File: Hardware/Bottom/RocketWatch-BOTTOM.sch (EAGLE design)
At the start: 31 parts, among them U1 AD5242-SO16

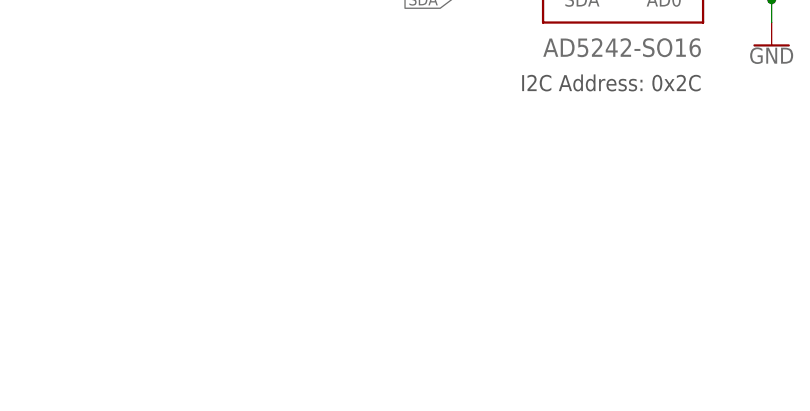
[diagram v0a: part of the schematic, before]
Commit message: changed schematic and board based on video take 002
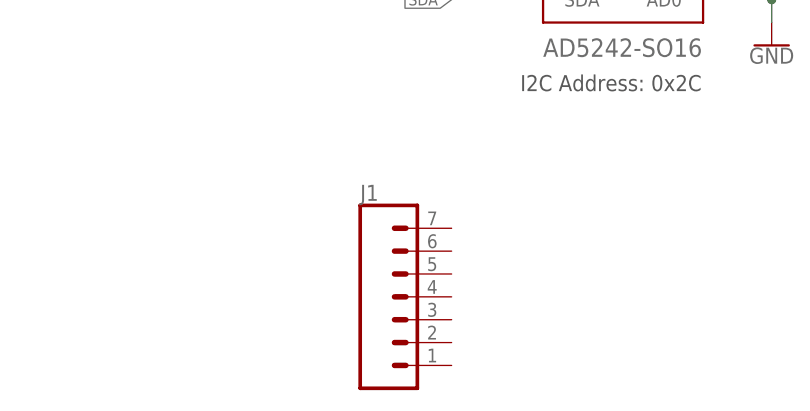
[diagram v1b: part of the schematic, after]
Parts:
- added J1: (no value), LinnesLab-Connectors:CONN_07
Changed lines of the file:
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@@
 <part name="GND30" library="LinnesLab-Symbols" deviceset="GND" device=""/>
 <part name="SUPPLY24" library="LinnesLab-Symbols" deviceset="3.3V" device=""/>
+<part name="J1" library="LinnesLab-Connectors" deviceset="CONN_07" device=""/>
 </parts>
 <sheets>
@@
 <attribute name="VALUE" x="68.58" y="-9.906" size="1.778" layer="96" align="bottom-center"/>
 </instance>
+<instance part="J1" gate="G$1" x="175.26" y="-22.86" smashed="yes">
+<attribute name="VALUE" x="170.18" y="-32.766" size="1.778" layer="96" font="vector"/>
+<attribute name="NAME" x="170.18" y="-9.652" size="1.778" layer="95" font="vector"/>
+</instance>
 </instances>

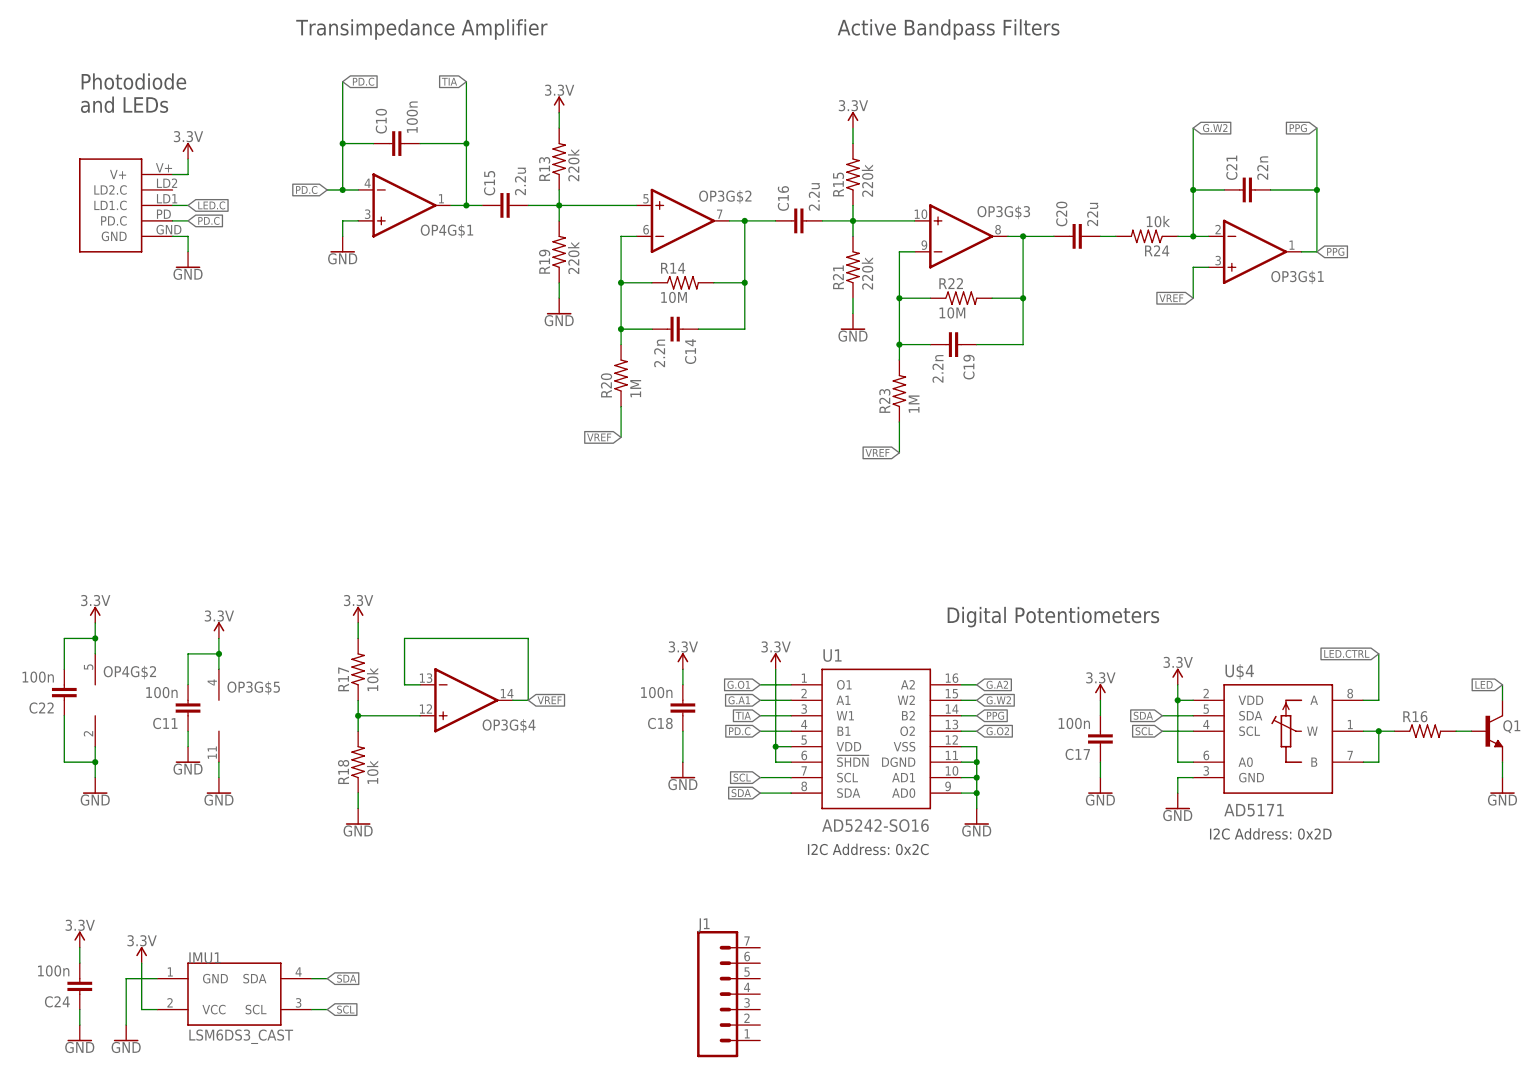
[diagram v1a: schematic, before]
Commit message: changes to top and bottom board based on take 002 video. Basic schematic and board is complete (no routing done yet)
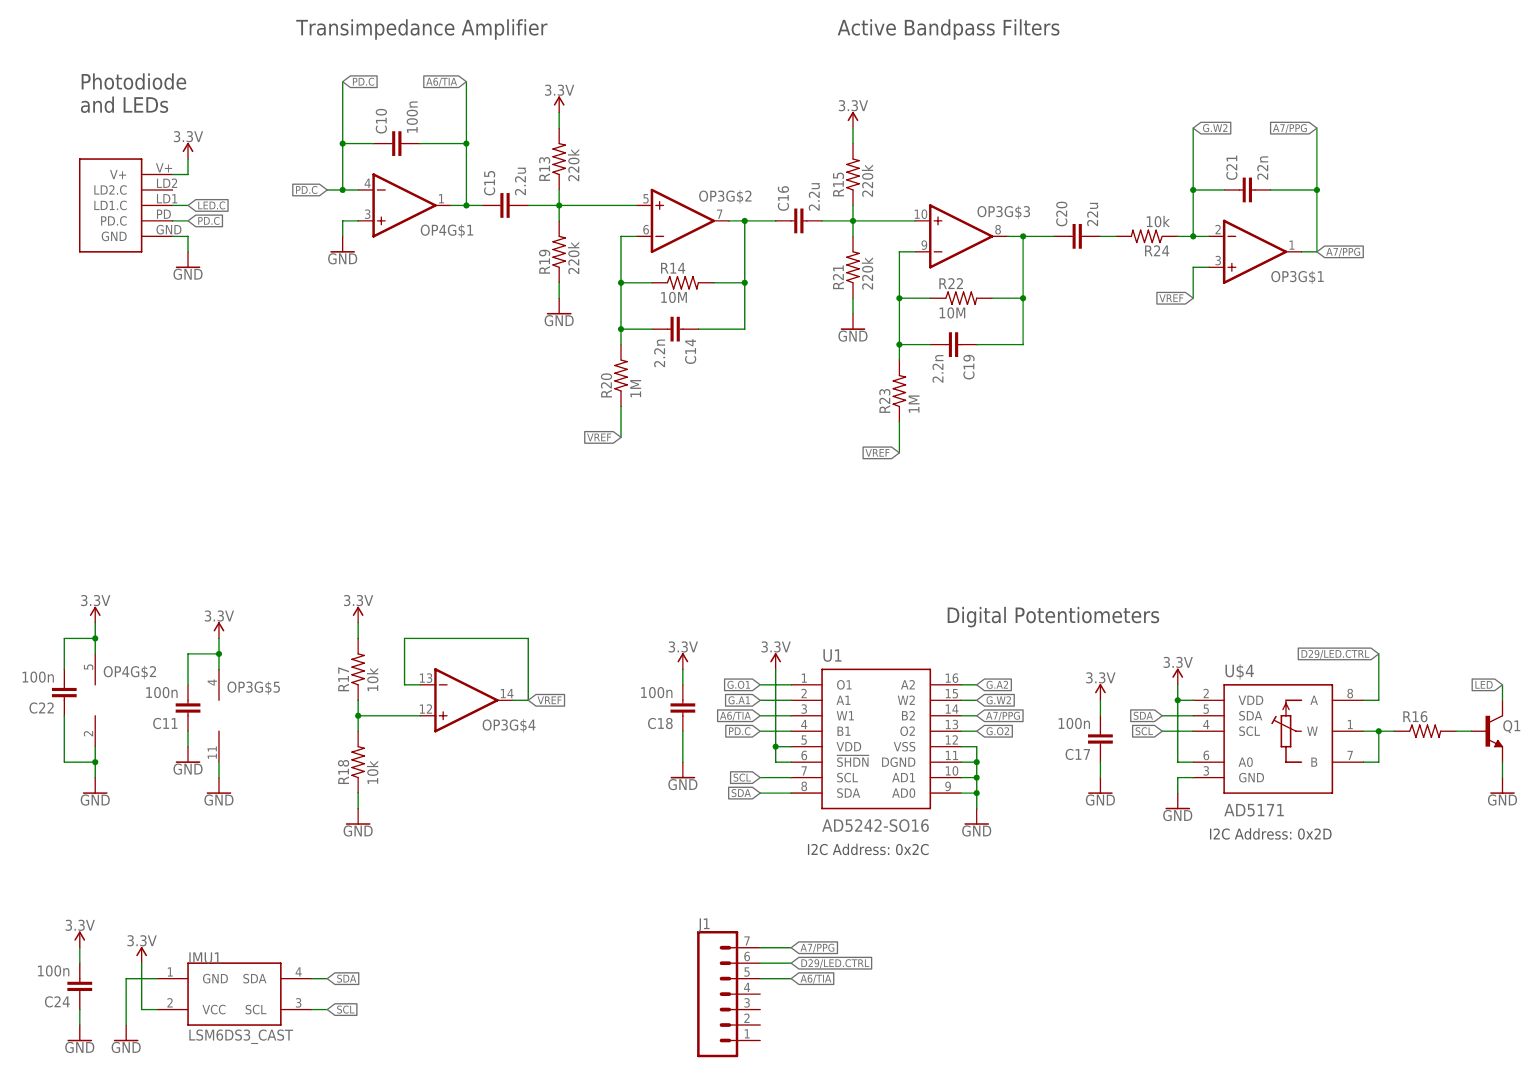
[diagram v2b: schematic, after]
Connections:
- removed net LED.CTRL: U$4.A
- removed net PPG: C21.2, OP3G$1.OUT, U1.B2
- removed net TIA: C10.2, C15.1, OP4G$1.OUT, U1.W1
- new net A6/TIA: C10.2, C15.1, J1.5, OP4G$1.OUT, U1.W1
- new net A7/PPG: C21.2, J1.7, OP3G$1.OUT, U1.B2
- new net D29/LED.CTRL: J1.6, U$4.A
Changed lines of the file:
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@@
 </segment>
 </net>
-<net name="TIA" class="0">
+<net name="A6/TIA" class="0">
 <segment>
 <wire x1="185.42" y1="25.4" x2="180.34" y2="25.4" width="0.1524" layer="91"/>
@@
 <junction x="132.08" y="109.22"/>
 </segment>
+<segment>
+<pinref part="J1" gate="G$1" pin="5"/>
+<wire x1="180.34" y1="-17.78" x2="185.42" y2="-17.78" width="0.1524" layer="91"/>
+<label x="185.42" y="-17.78" size="1.27" layer="95" xref="yes"/>
+</segment>
 </net>
 <net name="PD.C" class="0">
@@
 </segment>
 </net>
-<net name="LED.CTRL" class="0">
+<net name="D29/LED.CTRL" class="0">
 <segment>
 <pinref part="U$4" gate="G$1" pin="A"/>
@@
 <wire x1="281.94" y1="27.94" x2="281.94" y2="35.56" width="0.1524" layer="91"/>
 <label x="281.94" y="35.56" size="1.27" layer="95" rot="R180" xref="yes"/>
+</segment>
+<segment>
+<pinref part="J1" gate="G$1" pin="6"/>
+<wire x1="180.34" y1="-15.24" x2="185.42" y2="-15.24" width="0.1524" layer="91"/>
+<label x="185.42" y="-15.24" size="1.27" layer="95" xref="yes"/>
 </segment>
 </net>
@@
 </segment>
 </net>
-<net name="PPG" class="0">
+<net name="A7/PPG" class="0">
 <segment>
 <wire x1="213.36" y1="25.4" x2="215.9" y2="25.4" width="0.1524" layer="91"/>
@@
 <label x="271.78" y="101.6" size="1.27" layer="95" xref="yes"/>
 </segment>
-</net>
+<segment>
+<pinref part="J1" gate="G$1" pin="7"/>
+<wire x1="180.34" y1="-12.7" x2="185.42" y2="-12.7" width="0.1524" layer="91"/>
+<label x="185.42" y="-12.7" size="1.27" layer="95" xref="yes"/>
+</segment>
+</net>

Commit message: most of the bottom board routed. Few things left to route and clean up to show all labels.
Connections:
- removed net LED: Q1.C
- net LED.C: now also Q1.C
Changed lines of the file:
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@@
 <label x="86.36" y="109.22" size="1.27" layer="95" xref="yes"/>
+</segment>
+<segment>
+<wire x1="302.26" y1="27.94" x2="302.26" y2="30.48" width="0.1524" layer="91"/>
+<label x="302.26" y="30.48" size="1.27" layer="95" rot="R180" xref="yes"/>
+<pinref part="Q1" gate="G$1" pin="C"/>
 </segment>
 </net>
@@
 </segment>
 </net>
-<net name="LED" class="0">
-<segment>
-<wire x1="302.26" y1="27.94" x2="302.26" y2="30.48" width="0.1524" layer="91"/>
-<label x="302.26" y="30.48" size="1.27" layer="95" rot="R180" xref="yes"/>
-<pinref part="Q1" gate="G$1" pin="C"/>
-</segment>
-</net>
